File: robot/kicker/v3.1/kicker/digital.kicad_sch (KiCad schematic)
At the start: 65 parts, among them J2 Conn_ARM_JTAG_SWD_10, J3 Conn_01x02, J4 Conn_01x04_Pin, J4 Conn_01x10, P1 USB_C_Plug_USB2.0, Q4 BSS138K, SW1 BTN0, SW1 RST, SW3 SW_DIP_x04, U4 STM32F407VETx, U5 AT25DF041x-UxN-x, U6 SK9822, U7 SK9822, U8 AD8494

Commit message: Update power entry and regulation
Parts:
- C22, C23, C28, C29, C30, C31, C33, C34, C35, C38, C40, C41: LCSC C307331 -> (none)
- C24, C25, C26, C27, C36: LCSC C368809 -> (none)
- C32: LCSC C1518208 -> (none)
- C37, C39: LCSC C327009 -> (none)
- C42: LCSC C315248 -> (none)
- D10, D11: LCSC C5197644 -> (none)
- D12: LCSC C2984266 -> (none)
- D13: LCSC C72038 -> (none)
- D9: LCSC C2831531 -> (none)
- J3: LCSC C160402 -> (none)
- L6: LCSC C85833 -> (none)
- P1: LCSC C134092 -> (none)
- Q4: LCSC C112239 -> (none)
- R19, R36, R41, R42, R43, R44, R47, R50, R51, R52, R53, R54, R55: LCSC C60490 -> (none)
- R37, R38, R39, R40, R45: LCSC C12246 -> (none)
- R46: LCSC C60491 -> (none)
- R48: LCSC C25905 -> (none)
- R49: LCSC C26083 -> (none)
- SW1: LCSC C455243 -> (none)
- U4: LCSC C28730 -> (none)
- U6, U7: LCSC C2829089 -> (none)

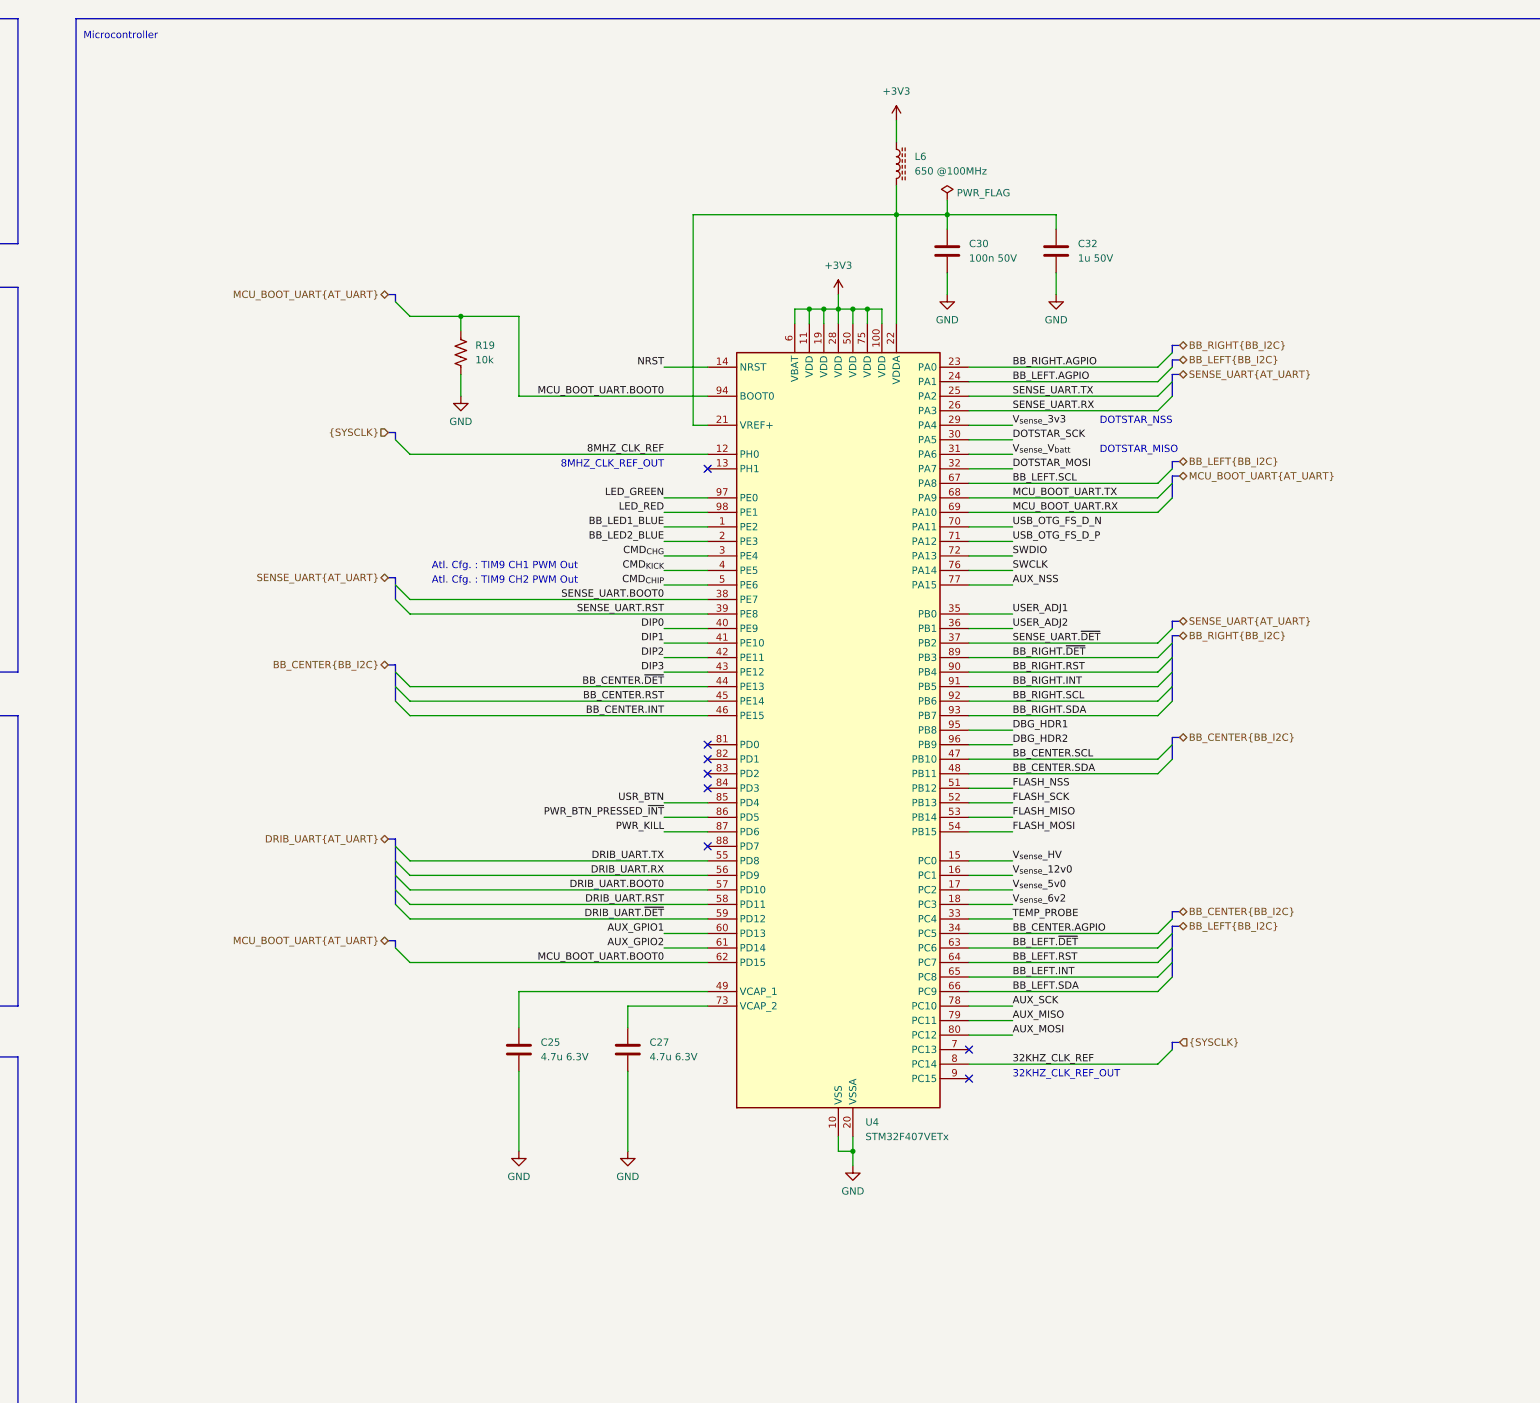
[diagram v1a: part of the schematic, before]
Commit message: Add local crystals
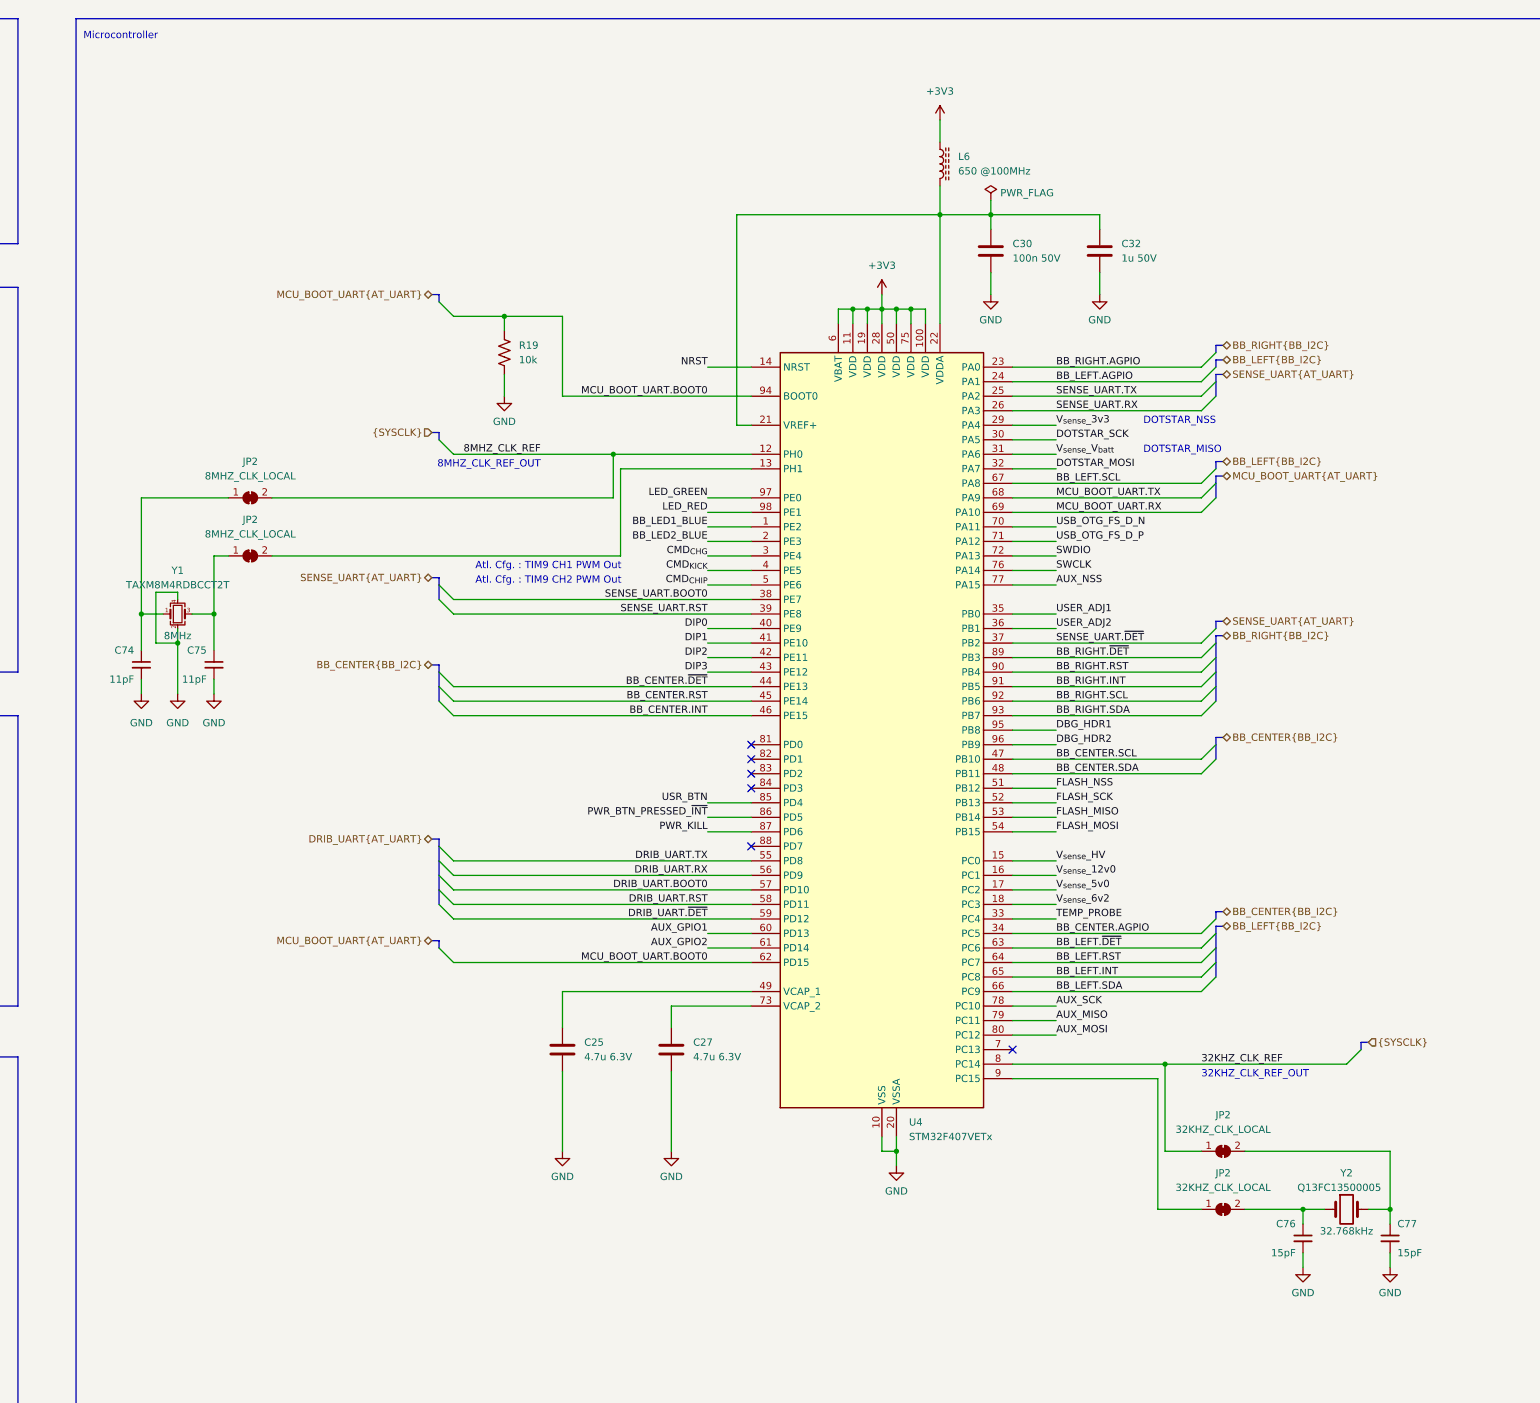
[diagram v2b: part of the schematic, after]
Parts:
- added C74, C75: 11pF, Capacitor_SMD:C_0402_1005Metric, symbol Device:C_Small
- added C76, C77: 15pF, Capacitor_SMD:C_0402_1005Metric, symbol Device:C_Small
- added JP2 (x2): 32KHZ_CLK_LOCAL, AT-BoardFeatures:SolderJumper-2_2.0x1.2mm_Closed, symbol Jumper:SolderJumper_2_Bridged
- added JP2 (x2): 8MHZ_CLK_LOCAL, AT-BoardFeatures:SolderJumper-2_2.0x1.2mm_Closed, symbol Jumper:SolderJumper_2_Bridged
- added Y1: TAXM8M4RDBCCT2T, Crystal:Crystal_SMD_3225-4Pin_3.2x2.5mm, symbol Device:Crystal_GND24_Small
- added Y2: Q13FC13500005, Crystal:Crystal_SMD_3215-2Pin_3.2x1.5mm, symbol Device:Crystal
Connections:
- net 32KHZ_CLK_REF: now also JP2.1 (A)
- net 8MHZ_CLK_REF: now also JP2.2 (B)
- net GND: now also C74.2, C75.2, C76.2, C77.2, Y1.2, Y1.4
- net at U4.13 (PH1): now also JP2.2 (B)
- net at U4.9 (PC15): now also JP2.1 (A)
- new net: C76.1, JP2.2 (B), Y2.1
- new net: C75.1, JP2.1 (A), Y1.3
- new net: C74.1, JP2.1 (A), Y1.1
- new net: C77.1, JP2.2 (B), Y2.2
- no-connect marks 14 -> 12
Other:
- moved on the sheet: C25, C27, C30, C32, L6, R19, U4

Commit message: Add power status LEDs and resolved ERC errors
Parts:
- added D19: XL-1608UOC-06, AT-LED:LED0603, symbol Device:LED
- added R103: 10k, Resistor_SMD:R_0402_1005Metric, symbol Device:R_Small_US
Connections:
- net GND: now also D19.1 (K)
- net ShutdownInitiated: now reaches U4.88 (PD7)
- net ShutdownInitiated: now also R103.1
- new net: D19.2 (A), R103.2
- no-connect marks 12 -> 11
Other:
- moved on the sheet: C36, D10, D11, D12, D13, R52, R53, R54, R55, U6, U7

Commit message: WIP
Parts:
- renumbered C22 to C26, C74 to C27, C75 to C28, C23 to C29, C24 to C30, C25 to C31, C26 to C32, C27 to C33, C28 to C34, C29 to C35, C31 to C36, C30 to C37, C33 to C38, C32 to C39, C34 to C40, C35 to C41, C76 to C42, C77 to C43, C36 to C44, C37 to C45, C38 to C46, C39 to C47, C40 to C48, C41 to C49, C42 to C50, D19 to D14, Q4 to Q5, R36 to R47, R37 to R48, R38 to R49, R39 to R50, R40 to R51, R41 to R52, R42 to R53, R43 to R54, R44 to R55, R45 to R56, R46 to R57, R47 to R58, R19 to R59, R48 to R60, R52 to R61, R49 to R62, R50 to R63, R51 to R64, R53 to R65, R54 to R66, R55 to R67, R103 to R68, U4 to U5, U5 to U7, U7 to U8, U8 to U9

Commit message: Kicker v3.1
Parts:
- C39: value 1u 50V -> 1u 50V
- C45, C47: value 10n 6.3V -> 10n 50V
- D10, D11: value Blue -> XL-1608UBC-04; Value2 (none) -> Blue
- D12: value Green -> XL-1608UGC-04; Value2 (none) -> Green
- D13: value Red -> XL-1608SURC-06; Value2 (none) -> Red
- J4, JP2, JP7, R58, U7, U9: now left out of the parts list
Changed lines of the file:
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@@
   (title_block
     (title "Kicker")
-    (date "2024-05-23")
+    (date "2024-06-10")
     (rev "3.1")
     (company "The A-Team (RC SSL)")
@@
       (effects (font (size 1.27 1.27)) (justify right))
     )
-    (property "Value" "10n 6.3V" (at 496.57 237.49 0)
+    (property "Value" "10n 50V" (at 496.57 237.49 0)
       (effects (font (size 1.27 1.27)) (justify right))
     )
@@
   )
   (symbol (lib_id "Sensor_Temperature:AD8494") (at 529.59 223.52 0) (unit 1)
-    (in_bom yes) (on_board yes) (dnp yes) (fields_autoplaced)
+    (in_bom no) (on_board yes) (dnp yes) (fields_autoplaced)
     (property "Reference" "U9" (at 542.29 219.3291 0)
       (effects (font (size 1.27 1.27)))
@@
   )
   (symbol (lib_id "Jumper:SolderJumper_2_Bridged") (at 295.91 228.6 0) (mirror x) (unit 1)
-    (in_bom yes) (on_board yes) (dnp no)
+    (in_bom no) (on_board yes) (dnp no)
     (property "Reference" "JP2" (at 295.91 222.25 0)
       (effects (font (size 1.27 1.27)))
@@
   )
   (symbol (lib_id "Device:LED") (at 462.28 82.55 90) (unit 1)
-    (in_bom yes) (on_board yes) (dnp no) (fields_autoplaced)
+    (in_bom yes) (on_board yes) (dnp no)
     (property "Reference" "D10" (at 466.09 82.8674 90)
       (effects (font (size 1.27 1.27)) (justify right))
     )
-    (property "Value" "Blue" (at 466.09 85.4074 90)
-      (effects (font (size 1.27 1.27)) (justify right))
+    (property "Value" "XL-1608UBC-04" (at 459.74 82.55 0)
+      (effects (font (size 1.27 1.27)))
     )
     (property "Footprint" "AT-LED:LED0603" (at 462.28 82.55 0)
@@
       (effects (font (size 1.27 1.27)) hide)
     )
+    (property "Value2" "Blue" (at 466.09 85.09 90)
+      (effects (font (size 1.27 1.27)) (justify right))
+    )
     (pin "1")
     (pin "2")
@@
   )
   (symbol (lib_id "Device:R_Small_US") (at 82.55 355.6 0) (unit 1)
-    (in_bom yes) (on_board yes) (dnp yes) (fields_autoplaced)
+    (in_bom no) (on_board yes) (dnp yes) (fields_autoplaced)
     (property "Reference" "R58" (at 85.09 354.33 0)
       (effects (font (size 1.27 1.27)) (justify left))
@@
   )
   (symbol (lib_id "Jumper:SolderJumper_2_Bridged") (at 125.73 104.14 0) (mirror x) (unit 1)
-    (in_bom yes) (on_board yes) (dnp no)
+    (in_bom no) (on_board yes) (dnp no)
     (property "Reference" "JP2" (at 125.73 97.79 0)
       (effects (font (size 1.27 1.27)))
@@
   )
   (symbol (lib_id "Connector:Conn_01x04_Pin") (at 539.75 349.25 0) (unit 1)
-    (in_bom yes) (on_board yes) (dnp yes) (fields_autoplaced)
+    (in_bom no) (on_board yes) (dnp yes) (fields_autoplaced)
     (property "Reference" "J4" (at 540.385 341.63 0)
       (effects (font (size 1.27 1.27)))
@@
   )
   (symbol (lib_id "Device:LED") (at 502.92 82.55 90) (unit 1)
-    (in_bom yes) (on_board yes) (dnp no) (fields_autoplaced)
+    (in_bom yes) (on_board yes) (dnp no)
     (property "Reference" "D12" (at 506.73 82.8674 90)
       (effects (font (size 1.27 1.27)) (justify right))
     )
-    (property "Value" "Green" (at 506.73 85.4074 90)
-      (effects (font (size 1.27 1.27)) (justify right))
+    (property "Value" "XL-1608UGC-04" (at 500.38 82.55 0)
+      (effects (font (size 1.27 1.27)))
     )
     (property "Footprint" "AT-LED:LED0603" (at 502.92 82.55 0)
@@
       (effects (font (size 1.27 1.27)) hide)
     )
+    (property "Value2" "Green" (at 506.73 85.09 90)
+      (effects (font (size 1.27 1.27)) (justify right))
+    )
     (pin "1")
     (pin "2")
@@
       (effects (font (size 1.27 1.27)) (justify right))
     )
-    (property "Value" " 1u 50V" (at 278.13 62.2299 0)
+    (property "Value" "1u 50V" (at 278.13 62.2299 0)
       (effects (font (size 1.27 1.27)) (justify right))
     )
@@
       (effects (font (size 1.27 1.27)) (justify right))
     )
-    (property "Value" "10n 6.3V" (at 496.57 212.09 0)
+    (property "Value" "10n 50V" (at 496.57 212.09 0)
       (effects (font (size 1.27 1.27)) (justify right))
     )
@@
   (symbol (lib_id "Device:LED") (at 548.64 82.55 90) (unit 1)
     (in_bom yes) (on_board yes) (dnp no)
-    (property "Reference" "D14" (at 552.45 80.01 90)
+    (property "Reference" "D14" (at 552.45 82.55 90)
       (effects (font (size 1.27 1.27)) (justify right))
     )
@@
       (effects (font (size 1.27 1.27)) hide)
     )
-    (property "Value2" "Orange" (at 552.45 82.55 90)
+    (property "Value2" "Orange" (at 552.45 85.09 90)
       (effects (font (size 1.27 1.27)) (justify right))
     )
@@
   )
   (symbol (lib_id "Device:LED") (at 520.7 82.55 90) (unit 1)
-    (in_bom yes) (on_board yes) (dnp no) (fields_autoplaced)
+    (in_bom yes) (on_board yes) (dnp no)
     (property "Reference" "D13" (at 524.51 82.8674 90)
       (effects (font (size 1.27 1.27)) (justify right))
     )
-    (property "Value" "Red" (at 524.51 85.4074 90)
-      (effects (font (size 1.27 1.27)) (justify right))
+    (property "Value" "XL-1608SURC-06" (at 518.16 82.55 0)
+      (effects (font (size 1.27 1.27)))
     )
     (property "Footprint" "AT-LED:LED0603" (at 520.7 82.55 0)
@@
       (effects (font (size 1.27 1.27)) hide)
     )
+    (property "Value2" "Red" (at 524.51 85.09 90)
+      (effects (font (size 1.27 1.27)) (justify right))
+    )
     (pin "1")
     (pin "2")
@@
   )
   (symbol (lib_id "Device:LED") (at 483.87 82.55 90) (unit 1)
-    (in_bom yes) (on_board yes) (dnp no) (fields_autoplaced)
+    (in_bom yes) (on_board yes) (dnp no)
     (property "Reference" "D11" (at 487.68 82.8674 90)
       (effects (font (size 1.27 1.27)) (justify right))
     )
-    (property "Value" "Blue" (at 487.68 85.4074 90)
-      (effects (font (size 1.27 1.27)) (justify right))
+    (property "Value" "XL-1608UBC-04" (at 481.33 82.55 0)
+      (effects (font (size 1.27 1.27)))
     )
     (property "Footprint" "AT-LED:LED0603" (at 483.87 82.55 0)
@@
       (effects (font (size 1.27 1.27)) hide)
     )
+    (property "Value2" "Blue" (at 487.68 85.09 90)
+      (effects (font (size 1.27 1.27)) (justify right))
+    )
     (pin "1")
     (pin "2")
@@
   )
   (symbol (lib_id "Jumper:SolderJumper_2_Bridged") (at 295.91 218.44 0) (mirror x) (unit 1)
-    (in_bom yes) (on_board yes) (dnp no)
+    (in_bom no) (on_board yes) (dnp no)
     (property "Reference" "JP2" (at 295.91 212.09 0)
       (effects (font (size 1.27 1.27)))
@@
   )
   (symbol (lib_id "Jumper:SolderJumper_2_Open") (at 115.57 374.65 90) (unit 1)
-    (in_bom yes) (on_board yes) (dnp no) (fields_autoplaced)
+    (in_bom no) (on_board yes) (dnp no) (fields_autoplaced)
     (property "Reference" "JP7" (at 118.11 373.3799 90)
       (effects (font (size 1.27 1.27)) (justify right))
@@
   )
   (symbol (lib_id "Jumper:SolderJumper_2_Bridged") (at 125.73 114.3 0) (mirror x) (unit 1)
-    (in_bom yes) (on_board yes) (dnp no)
+    (in_bom no) (on_board yes) (dnp no)
     (property "Reference" "JP2" (at 125.73 107.95 0)
       (effects (font (size 1.27 1.27)))
@@
   )
   (symbol (lib_id "Memory_Flash:AT25SF081-SSHD-X") (at 495.3 137.16 0) (unit 1)
-    (in_bom yes) (on_board yes) (dnp yes) (fields_autoplaced)
+    (in_bom no) (on_board yes) (dnp yes) (fields_autoplaced)
     (property "Reference" "U7" (at 504.19 135.89 0)
       (effects (font (size 1.27 1.27)) (justify left))
